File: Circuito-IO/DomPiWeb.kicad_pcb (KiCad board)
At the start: 2 copper layers, 90 x 55 mm, 84 parts, among them J1 Entrada 12v, J10 Bx3, J11 Bx2, J12 Bx3, J2 Salida 5v, J3 CONUFL001-SMD-T (Linx), J4 Salida 5v Controlada, J5 SIM7050, J6 RaspberryPi GPIO, J7 SIMDBG, J8 EXP1, J9 Bx2, Q1 DMG2305UXQ6, Q2 DMG2305UXQ6, U1 LM2596S-ADJ, U2 SIM900

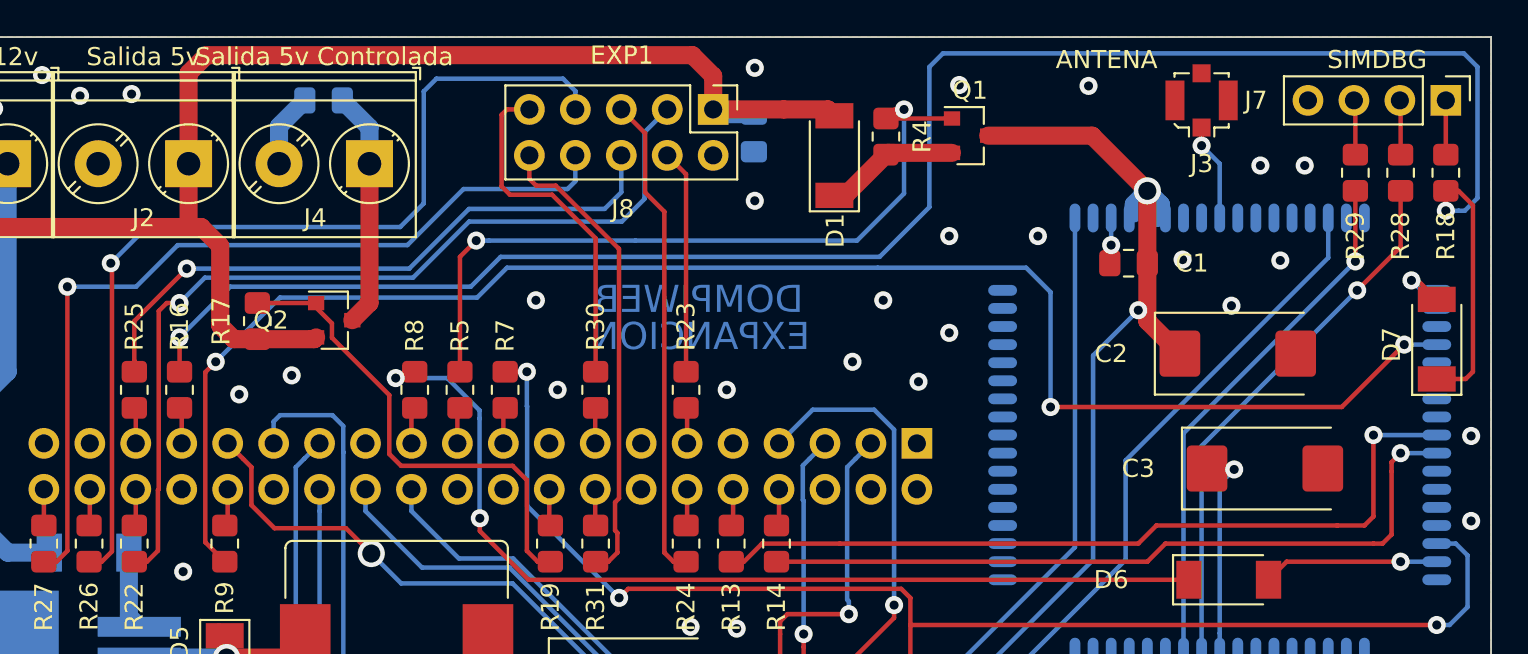
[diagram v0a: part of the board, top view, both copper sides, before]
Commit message: Correcciones a circuito y placa luego de prototipo
Correcciones a circuito y placa luego de prototipo
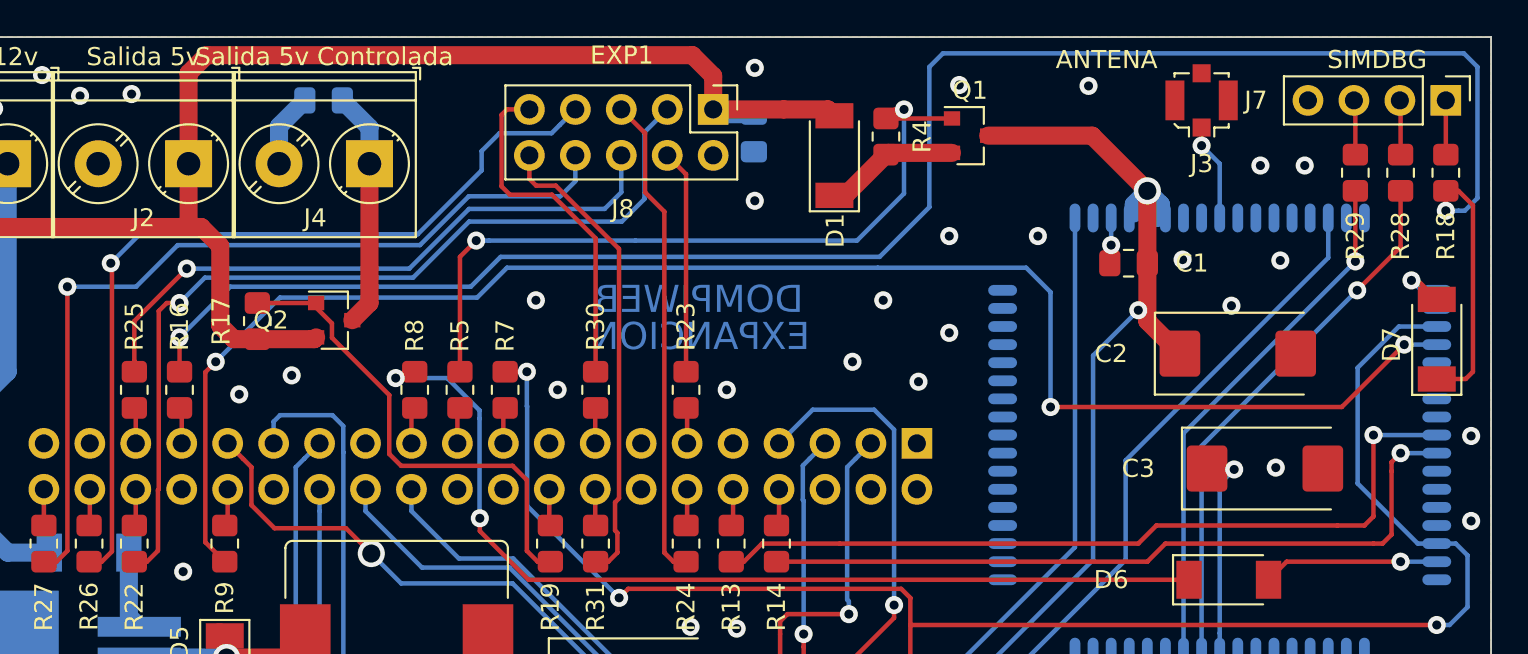
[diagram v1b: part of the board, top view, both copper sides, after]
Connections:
- U2 pad 3: GND -> Net-(R6-Pad1)
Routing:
- net Net-(R6-Pad1): track 79.6 -> 97.1 mm
- net Net-(J8-Pad7): track 52.3 -> 47.3 mm
- net GND: vias 45 -> 46
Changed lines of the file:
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@@
     (thickness 1.6)
     (drawings 20)
-    (tracks 625)
+    (tracks 630)
     (zones 0)
     (modules 84)
@@
       (net 73 "Net-(R9-Pad2)"))
     (pad 3 smd oval (at -12 6 180) (size 1.6 0.6) (layers B.Cu B.Paste B.Mask)
-      (net 1 GND))
+      (net 72 "Net-(R6-Pad1)"))
     (pad 2 smd oval (at -12 7 180) (size 1.6 0.6) (layers B.Cu B.Paste B.Mask)
       (net 113 "Net-(U2-Pad2)"))
@@
   (via (at 135.75 97.6) (size 1) (drill 0.5) (layers F.Cu B.Cu) (net 1))
   (via (at 138.3 97.7) (size 1) (drill 0.5) (layers F.Cu B.Cu) (net 1))
+  (via (at 168.1 88.8) (size 1) (drill 0.5) (layers F.Cu B.Cu) (net 1))
   (via (at 161 73.5) (size 1.5) (drill 1) (layers F.Cu B.Cu) (net 2))
   (segment (start 161.749999 74.750001) (end 161.5 75) (width 1) (layer B.Cu) (net 2))
@@
   (segment (start 101.3 93.4) (end 101.3 78.8) (width 0.25) (layer F.Cu) (net 65))
   (segment (start 129.38 72.97) (end 129.38 71.54) (width 0.25) (layer B.Cu) (net 65))
-  (segment (start 128.95 73.4) (end 129.38 72.97) (width 0.25) (layer B.Cu) (net 65))
-  (segment (start 123.2 73.4) (end 128.95 73.4) (width 0.25) (layer B.Cu) (net 65))
-  (segment (start 120.1 76.5) (end 123.2 73.4) (width 0.25) (layer B.Cu) (net 65))
-  (segment (start 107.4 76.5) (end 120.1 76.5) (width 0.25) (layer B.Cu) (net 65))
+  (segment (start 128.55 73.8) (end 129.38 72.97) (width 0.25) (layer B.Cu) (net 65))
+  (segment (start 123.49288 73.8) (end 128.55 73.8) (width 0.25) (layer B.Cu) (net 65))
+  (segment (start 120.79288 76.5) (end 123.49288 73.8) (width 0.25) (layer B.Cu) (net 65))
+  (segment (start 107.4 76.5) (end 120.79288 76.5) (width 0.25) (layer B.Cu) (net 65))
   (segment (start 105.1 78.8) (end 107.4 76.5) (width 0.25) (layer B.Cu) (net 65))
   (segment (start 101.3 78.8) (end 105.1 78.8) (width 0.25) (layer B.Cu) (net 65))
@@
   (segment (start 103.765001 77.565001) (end 103.7 77.5) (width 0.25) (layer F.Cu) (net 66))
   (segment (start 103.765001 93.434999) (end 103.765001 77.565001) (width 0.25) (layer F.Cu) (net 66))
-  (segment (start 121 68) (end 121.7 67.3) (width 0.25) (layer B.Cu) (net 66))
-  (segment (start 121 74.2) (end 121 68) (width 0.25) (layer B.Cu) (net 66))
-  (segment (start 119.7 75.5) (end 121 74.2) (width 0.25) (layer B.Cu) (net 66))
-  (segment (start 105.7 75.5) (end 119.7 75.5) (width 0.25) (layer B.Cu) (net 66))
-  (segment (start 103.7 77.5) (end 105.7 75.5) (width 0.25) (layer B.Cu) (net 66))
-  (segment (start 121.7 67.3) (end 128.7 67.3) (width 0.25) (layer B.Cu) (net 66))
-  (segment (start 128.7 67.3) (end 129.4 68) (width 0.25) (layer B.Cu) (net 66))
-  (segment (start 129.38 68.02) (end 129.38 69) (width 0.25) (layer B.Cu) (net 66))
-  (segment (start 129.4 68) (end 129.38 68.02) (width 0.25) (layer B.Cu) (net 66))
+  (segment (start 128.530001 69.849999) (end 129.38 69) (width 0.25) (layer B.Cu) (net 66))
+  (segment (start 125.185001 70.314999) (end 128.065001 70.314999) (width 0.25) (layer B.Cu) (net 66))
+  (segment (start 124.2 71.3) (end 125.185001 70.314999) (width 0.25) (layer B.Cu) (net 66))
+  (segment (start 128.065001 70.314999) (end 128.530001 69.849999) (width 0.25) (layer B.Cu) (net 66))
+  (segment (start 124.2 72.366998) (end 124.2 71.3) (width 0.25) (layer B.Cu) (net 66))
+  (segment (start 120.666998 75.9) (end 124.2 72.366998) (width 0.25) (layer B.Cu) (net 66))
+  (segment (start 105.3 75.9) (end 120.666998 75.9) (width 0.25) (layer B.Cu) (net 66))
+  (segment (start 103.7 77.5) (end 105.3 75.9) (width 0.25) (layer B.Cu) (net 66))
   (segment (start 105 83.5) (end 105 82.9) (width 0.25) (layer F.Cu) (net 67))
   (via (at 107.9 77.8) (size 1) (drill 0.5) (layers F.Cu B.Cu) (net 67))
@@
   (segment (start 147.9 97.5) (end 147.9 103.9) (width 0.25) (layer F.Cu) (net 72))
   (segment (start 147.9 96.004998) (end 147.9 97.5) (width 0.25) (layer F.Cu) (net 72))
+  (segment (start 175.95 93) (end 177 93) (width 0.25) (layer B.Cu) (net 72))
+  (segment (start 172.624999 89.674999) (end 175.95 93) (width 0.25) (layer B.Cu) (net 72))
+  (segment (start 172.624999 83.279999) (end 172.624999 89.674999) (width 0.25) (layer B.Cu) (net 72))
+  (segment (start 174.904998 81) (end 172.624999 83.279999) (width 0.25) (layer B.Cu) (net 72))
+  (segment (start 177 81) (end 174.904998 81) (width 0.25) (layer B.Cu) (net 72))
   (via (at 109.5 82.95) (size 1) (drill 0.5) (layers F.Cu B.Cu) (net 73))
   (segment (start 108.92499 83.52501) (end 109.5 82.95) (width 0.25) (layer F.Cu) (net 73))
@@
   (segment (start 133 113) (end 133 110) (width 1) (layer B.Cu) (net 120))
   (segment (start 128 113) (end 128 110) (width 1) (layer B.Cu) (net 121))
-  (zone (net 1) (net_name GND) (layer B.Cu) (hatch edge 0.508)
+  (zone (net 1) (net_name GND) (layer F.Cu) (hatch edge 0.508)
     (connect_pads (clearance 0.508))
     (min_thickness 0.254)
@@
     )
   )
-  (zone (net 1) (net_name GND) (layer F.Cu) (hatch edge 0.508)
+  (zone (net 1) (net_name GND) (layer B.Cu) (hatch edge 0.508)
     (connect_pads (clearance 0.508))
     (min_thickness 0.254)

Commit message: Rediseño y nueva version de KiCAD
Rediseño y nueva version de KiCAD
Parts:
- removed C1, C7: 100nf, Capacitor_SMD:C_0805_2012Metric_Pad1.18x1.45mm_HandSolder
- removed C2: 470uf, Capacitor_Tantalum_SMD:CP_EIA-7343-43_Kemet-X_Pad2.25x2.55mm_HandSolder
- removed C3: 4,7uf, Capacitor_Tantalum_SMD:CP_EIA-7343-43_Kemet-X_Pad2.25x2.55mm_HandSolder
- removed D4, D8, D9: Led SMD, LED_SMD:LED_1206_3216Metric_Pad1.42x1.75mm_HandSolder
- removed D6, D7: LL4148, Diode_SMD:D_SOD-128
- removed Q1: DMG2305UXQ6, Package_TO_SOT_SMD:SOT-23
- removed R10, R11, R12: 33, Resistor_SMD:R_0805_2012Metric_Pad1.20x1.40mm_HandSolder
- removed R15: 10K, Resistor_SMD:R_0805_2012Metric_Pad1.20x1.40mm_HandSolder
- removed R18, R20, R21, R28, R29, R5, R6, R7: 1K, Resistor_SMD:R_0805_2012Metric_Pad1.20x1.40mm_HandSolder
- removed U2: SIM900, RF_GSM:SIMCom_SIM900
- added C18: 100nf, Capacitor_SMD:C_0805_2012Metric_Pad1.18x1.45mm_HandSolder, F.Cu at (225.0, 99.0)
- added C19: 470uf, Capacitor_Tantalum_SMD:CP_EIA-7343-43_Kemet-X_Pad2.25x2.55mm_HandSolder, F.Cu at (244.9, 79.2)
- added J13: Bx2, TerminalBlock_Phoenix:TerminalBlock_Phoenix_PT-1,5-2-5.0-H_1x02_P5.00mm_Horizontal, F.Cu at (150.5, 113.0)
- added J14: Bx2, TerminalBlock_Phoenix:TerminalBlock_Phoenix_PT-1,5-2-5.0-H_1x02_P5.00mm_Horizontal, F.Cu at (160.5, 113.0)
- added K1: FINDER-36.11, Relay_THT:Relay_SPDT_Finder_36.11, F.Cu at (158.4, 98.5)
- added K2: FINDER-36.11, Relay_THT:Relay_SPDT_Finder_36.11, F.Cu at (158.4, 82.0)
- added Q3: BC848, Package_TO_SOT_SMD:SOT-23, F.Cu at (229.9, 95.3)
- added Q4: BC848, Package_TO_SOT_SMD:SOT-23, F.Cu at (242.2, 84.4)
- added Q5: BC848, Package_TO_SOT_SMD:SOT-23, F.Cu at (225.0, 95.3)
- added R41: 1K, Resistor_SMD:R_0805_2012Metric_Pad1.20x1.40mm_HandSolder, F.Cu at (234.8, 94.5)
- added R42: 1K, Resistor_SMD:R_0805_2012Metric_Pad1.20x1.40mm_HandSolder, F.Cu at (225.0, 102.0)
- added R43: 10K, Resistor_SMD:R_0805_2012Metric_Pad1.20x1.40mm_HandSolder, F.Cu at (225.0, 104.9)
- added R44: 10K, Resistor_SMD:R_0805_2012Metric_Pad1.20x1.40mm_HandSolder, F.Cu at (229.8, 99.0)
- D1: value M7 -> LL4148; footprint Diode_SMD:D_SOD-128 -> Diode_SMD:D_MiniMELF
- D2: value Led SMD -> LL4148; footprint LED_SMD:LED_1206_3216Metric_Pad1.42x1.75mm_HandSolder -> Diode_SMD:D_MiniMELF
- J3: value CONUFL001-SMD-T (Linx) -> Bx3; footprint Connector_Coaxial:U.FL_Molex_MCRF_73412-0110_Vertical -> TerminalBlock_Phoenix:TerminalBlock_Phoenix_PT-1,5-3-5.0-H_1x03_P5.00mm_Horizontal
- J5: value SIM7050 -> Bx2; footprint KiCAD:GCT_SIM7050-6-0-00-X_REVC -> TerminalBlock_Phoenix:TerminalBlock_Phoenix_PT-1,5-2-5.0-H_1x02_P5.00mm_Horizontal
- J7: value SIMDBG -> Bx3; footprint Connector_PinHeader_2.54mm:PinHeader_1x04_P2.54mm_Vertical -> TerminalBlock_Phoenix:TerminalBlock_Phoenix_PT-1,5-3-5.0-H_1x03_P5.00mm_Horizontal
- R1, R13, R14: value 1K -> 22R
- R16: value 1K -> 10K
- R4: value 10K -> 22R
- moved J7 65.6 mm to (199.0, 130.5), turned to 90 degrees
- moved J5 38.3 mm to (199.0, 115.5)
- moved J3 18.6 mm to (179.0, 57.5)
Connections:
- D1 pad 1: Net-(D1-Pad1) -> Net-(C18-Pad1)
- D1 pad 2: +5VD -> Net-(Q5-Pad3)
- D2 pad 1: GND -> Net-(C18-Pad1)
- D2 pad 2: Net-(D2-Pad2) -> Net-(Q4-Pad3)
- D3 pad 1: Net-(D3-Pad1) -> Net-(C18-Pad1)
- J3 pad 1: Net-(J3-Pad1) -> GND
- J3 pad 2: GND -> Net-(R14-Pad2)
- J5 pad 1: (no net) -> Net-(J5-Pad1)
- J5 pad 2: (no net) -> +5VD
- J6 pad 1: Net-(J6-Pad1) -> unconnected-(J6-Pad1)
- J6 pad 13: Net-(J6-Pad13) -> unconnected-(J6-Pad13)
- J6 pad 17: Net-(J6-Pad17) -> unconnected-(J6-Pad17)
- J6 pad 2: Net-(J6-Pad2) -> unconnected-(J6-Pad2)
- J6 pad 22: Net-(J6-Pad22) -> unconnected-(J6-Pad22)
- J6 pad 37: Net-(J6-Pad37) -> unconnected-(J6-Pad37)
- J6 pad 4: Net-(J6-Pad4) -> unconnected-(J6-Pad4)
- J7 pad 1: Net-(J7-Pad1) -> GND
- J7 pad 2: Net-(J7-Pad2) -> Net-(R9-Pad2)
- R1 pad 1: Net-(D2-Pad2) -> Net-(J6-Pad21)
- R1 pad 2: Net-(C1-Pad2) -> Net-(J5-Pad1)
- R16 pad 1: Net-(J6-Pad33) -> GND
- R19 pad 1: Net-(Q2-Pad1) -> Net-(Q3-Pad3)
- R19 pad 2: Net-(J6-Pad18) -> Net-(Q2-Pad1)
- R4 pad 1: Net-(Q1-Pad1) -> Net-(J6-Pad19)
- R4 pad 2: Net-(D1-Pad1) -> Net-(J7-Pad3)
- U1 pad 1: Net-(D3-Pad1) -> Net-(C18-Pad1)
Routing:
- net Net-(R6-Pad1): track 97.1 -> 0.00 mm, vias 4 -> 0
- net Net-(C1-Pad2): track 63.7 -> 0.00 mm, vias 2 -> 0
- net Net-(Q3-Pad1): track 108.6 -> 55.1 mm, vias 2 -> 1
- net Net-(R20-Pad1): track 49.2 -> 0.00 mm
- net Net-(Q1-Pad1): track 41.9 -> 0.00 mm, vias 2 -> 0
- net Net-(R14-Pad2): track 41.3 -> 0.00 mm, vias 1 -> 0
- net Net-(R21-Pad1): track 40.4 -> 0.00 mm
- net Net-(R9-Pad2): track 89.7 -> 50.5 mm, vias 3 -> 1
- net Net-(J6-Pad19): track 2.20 -> 40.4 mm, vias 0 -> 2
- net Net-(R13-Pad2): track 44.5 -> 6.41 mm, vias 1 -> 0
- net Net-(Q5-Pad1): track 53.2 -> 16.7 mm
- net (no net): track 0.00 -> 31.6 mm, vias 0 -> 2
- net Net-(R28-Pad2): track 30.1 -> 0.00 mm, vias 1 -> 0
- net Net-(R29-Pad2): track 29.4 -> 0.00 mm, vias 1 -> 0
- net Net-(C7-Pad1): track 24.8 -> 0.00 mm, vias 2 -> 0
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- removed copper zone on B.Cu, net GND
- removed copper zone on F.Cu, net GND
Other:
- net class 1mm removed
- net class Default removed
- board text removed: "ANTENA"
- board text removed: "SIM"

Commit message: Placa para central con relee y sin modem
Placa para central con relee y sin modem
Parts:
- removed J7: Bx3, TerminalBlock_Phoenix:TerminalBlock_Phoenix_PT-1,5-3-5.0-H_1x03_P5.00mm_Horizontal
- C6, C8, D3, R1, R32, R33, R34, R35, R36, R37, R38, R39, R40, U1: moved to F.Cu
- J3: value Bx3 -> Serial; footprint TerminalBlock_Phoenix:TerminalBlock_Phoenix_PT-1,5-3-5.0-H_1x03_P5.00mm_Horizontal -> Connector_PinHeader_2.54mm:PinHeader_1x03_P2.54mm_Vertical
- J5: value Bx2 -> EXP2; footprint TerminalBlock_Phoenix:TerminalBlock_Phoenix_PT-1,5-2-5.0-H_1x02_P5.00mm_Horizontal -> Connector_PinHeader_2.54mm:PinHeader_1x05_P2.54mm_Vertical
- R9: value 1K -> 22R
- moved R42 113.7 mm to (112.5, 85.0)
- moved R32 84.3 mm to (60.8, 92.6), turned to 0 degrees
- moved C8 80.8 mm to (60.8, 89.7), turned to 0 degrees
- moved R39 78.0 mm to (55.3, 102.0), turned to 0 degrees
- moved R40 74.9 mm to (65.6, 89.6), turned to 0 degrees
- moved C6 73.1 mm to (50.5, 102.0), turned to 0 degrees
- moved R38 68.5 mm to (60.8, 95.6), turned to 0 degrees
- moved R37 59.7 mm to (65.6, 92.6), turned to 0 degrees
- moved D3 58.8 mm to (44.4, 102.5), turned to 0 degrees
- moved C19 53.7 mm to (192.2, 89.5)
- moved Q4 53.7 mm to (189.5, 94.7)
- moved R35 53.2 mm to (60.8, 98.5), turned to 0 degrees
- moved J5 51.7 mm to (177.5, 68.5), turned to -90 degrees
- moved R36 51.4 mm to (70.4, 89.6), turned to 0 degrees
- moved U1 50.4 mm to (49.6, 94.3), turned to 0 degrees
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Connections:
- J3 pad 1: GND -> Net-(R13-Pad2)
- J3 pad 3: Net-(R13-Pad2) -> GND
- J5 pad 1: Net-(J5-Pad1) -> +5VD
- J5 pad 2: +5VD -> Net-(R1-Pad2)
- R1 pad 2: Net-(J5-Pad1) -> Net-(R1-Pad2)
- R4 pad 2: Net-(J7-Pad3) -> Net-(R4-Pad2)
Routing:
- net +5VD: track 168.8 -> 0.00 mm
- net Net-(C15-Pad1): track 59.0 -> 0.00 mm, vias 2 -> 0
- net Net-(C13-Pad1): track 56.1 -> 0.00 mm, vias 2 -> 0
- net Net-(Q3-Pad1): track 55.1 -> 0.00 mm, vias 1 -> 0
- net Net-(C14-Pad1): track 50.6 -> 0.00 mm, vias 2 -> 0
- net Net-(R9-Pad2): track 50.5 -> 0.00 mm, vias 1 -> 0
- net Net-(J8-Pad3): track 49.7 -> 0.00 mm, vias 1 -> 0
- net Net-(J8-Pad8): track 48.1 -> 0.00 mm, vias 1 -> 0
- net Net-(J8-Pad7): track 47.3 -> 0.00 mm, vias 1 -> 0
- net Net-(C12-Pad1): track 45.9 -> 0.00 mm
- net Net-(C11-Pad1): track 45.1 -> 0.00 mm, vias 1 -> 0
- net Net-(J6-Pad19): track 40.4 -> 0.00 mm, vias 2 -> 0
- net Net-(C10-Pad1): track 38.4 -> 0.00 mm
- net Net-(C17-Pad1): track 37.3 -> 0.00 mm
- net Net-(J8-Pad6): track 35.3 -> 0.00 mm, vias 1 -> 0
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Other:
- board text removed: "DOMPIWEB"
- board text removed: "EXPANCION"

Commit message: Update
Update
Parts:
- U1: moved to B.Cu
- moved C19 97.7 mm to (94.5, 88.5), turned to 90 degrees
- moved C18 93.1 mm to (100.5, 83.0)
- moved R35 85.8 mm to (145.5, 84.5), turned to -90 degrees
- moved R37 75.4 mm to (140.5, 84.5), turned to -90 degrees
- moved C6 73.1 mm to (120.0, 79.5)
- moved R41 73.0 mm to (128.0, 93.0), turned to -90 degrees
- moved R36 72.8 mm to (143.0, 84.5), turned to -90 degrees
- moved Q3 71.9 mm to (127.5, 79.0)
- moved R32 59.2 mm to (120.0, 93.0), turned to 90 degrees
- moved R39 57.4 mm to (110.0, 84.5), turned to -90 degrees
- moved R34 55.7 mm to (115.0, 93.0), turned to 90 degrees
- moved D3 54.9 mm to (94.5, 80.0), turned to 180 degrees
- moved R38 52.9 mm to (112.5, 84.5), turned to -90 degrees
- moved R40 52.0 mm to (117.5, 93.0), turned to 90 degrees
- moved R33 50.7 mm to (115.0, 84.5), turned to -90 degrees
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
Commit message: Update
Update
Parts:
- C6, C8: moved to B.Cu
- J13: value Bx2 -> Salida 1
- J14: value Bx2 -> Salida 2
- moved R17 21.7 mm to (129.5, 67.0), turned to 180 degrees
- moved R4 17.7 mm to (110.0, 93.0), turned to -90 degrees
- moved R42 15.5 mm to (123.0, 84.5)
- moved Q2 14.2 mm to (127.0, 70.5), turned to 180 degrees
- moved J8 11.5 mm to (148.5, 68.5)
- moved R19 11.3 mm to (131.0, 70.5)
- moved R9 8.86 mm to (107.5, 84.5), turned to 90 degrees
- moved R16 6.10 mm to (126.5, 75.5)
- moved C6 6.02 mm to (115.5, 75.5), turned to 180 degrees
- moved Q3 4.61 mm to (130.5, 75.5)
- moved D1 4.47 mm to (156.5, 102.5)
- moved D2 4.03 mm to (156.5, 85.5)
- moved R43 3.54 mm to (157.5, 80.5)
- moved R44 3.35 mm to (157.5, 97.0)
- moved R1 2.50 mm to (125.5, 84.5)
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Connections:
- R1 pad 1: Net-(J6-Pad21) -> Net-(J6-Pad19)
- R4 pad 1: Net-(J6-Pad19) -> Net-(J6-Pad32)
- R42 pad 1: Net-(J6-Pad33) -> Net-(J6-Pad21)
- R9 pad 1: Net-(J6-Pad32) -> Net-(J6-Pad33)
